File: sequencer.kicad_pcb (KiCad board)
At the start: 2 copper layers, 171.4 x 106.7 mm, 435 parts, among them J1 PJ301CM, J10 PJ301BM, J11 PJ301BM, J12 PJ301BM, J13 PJ301BM, J14 PJ301BM, J15 PJ301BM, J16 PJ301BM, J17 PJ301BM, J18 PJ301BM, J19 PJ301BM, J2 PJ301CM, J20 PJ301BM, J21 PJ301BM, J22 PJ301BM, J23 PJ301BM, J24 PJ301BM, J25 PJ301BM, J26 PJ301BM, J3 PJ301BM, J4 PJ301BM, J5 PJ301BM, J6 PJ301BM, J7 PJ301BM, J8 PJ301BM, J9 PJ301BM, Q1 MMBT3904, Q2 MMBT3904, Q3 MMBT3904, Q4 MMBT3904, Q5 MMBT3904, SW1 TL1105, SW10 TL1105, SW11 TL1105, SW12 TL1105, SW13 TL1105, SW14 TL1105, SW15 TL1105, SW16 TL1105, SW17 TL1105, SW18 TL1105, SW19 EVQQ2, SW2 TL1105, SW20 TL1105, SW21 TL1105, SW22 TL1105, SW23 TL1105, SW24 TL1105, SW25 TL1105, SW26 TL1105, SW27 TL1105, SW28 TL1105, SW29 TL1105, SW3 TL1105, SW30 TL1105, SW31 TL1105, SW32 TL1105, SW33 TL1105, SW34 TL1105, SW35 TL1105, SW36 TL1105, SW37 TL1105, SW38 TL1105, SW39 TL1105, SW4 TL1105, SW5 TL1105, SW6 TL1105, SW7 TL1105, SW8 EVQQ2, SW9 TL1105, U1 VO0600T, U10 LM1117-3.3, U11 74HC165, U12 74HC595, U13 74HC595, U14 74HC595, U15 OPA4172, U16 R-78E5.0-1.0, U2 74LV1T34, U3 STMPS2151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

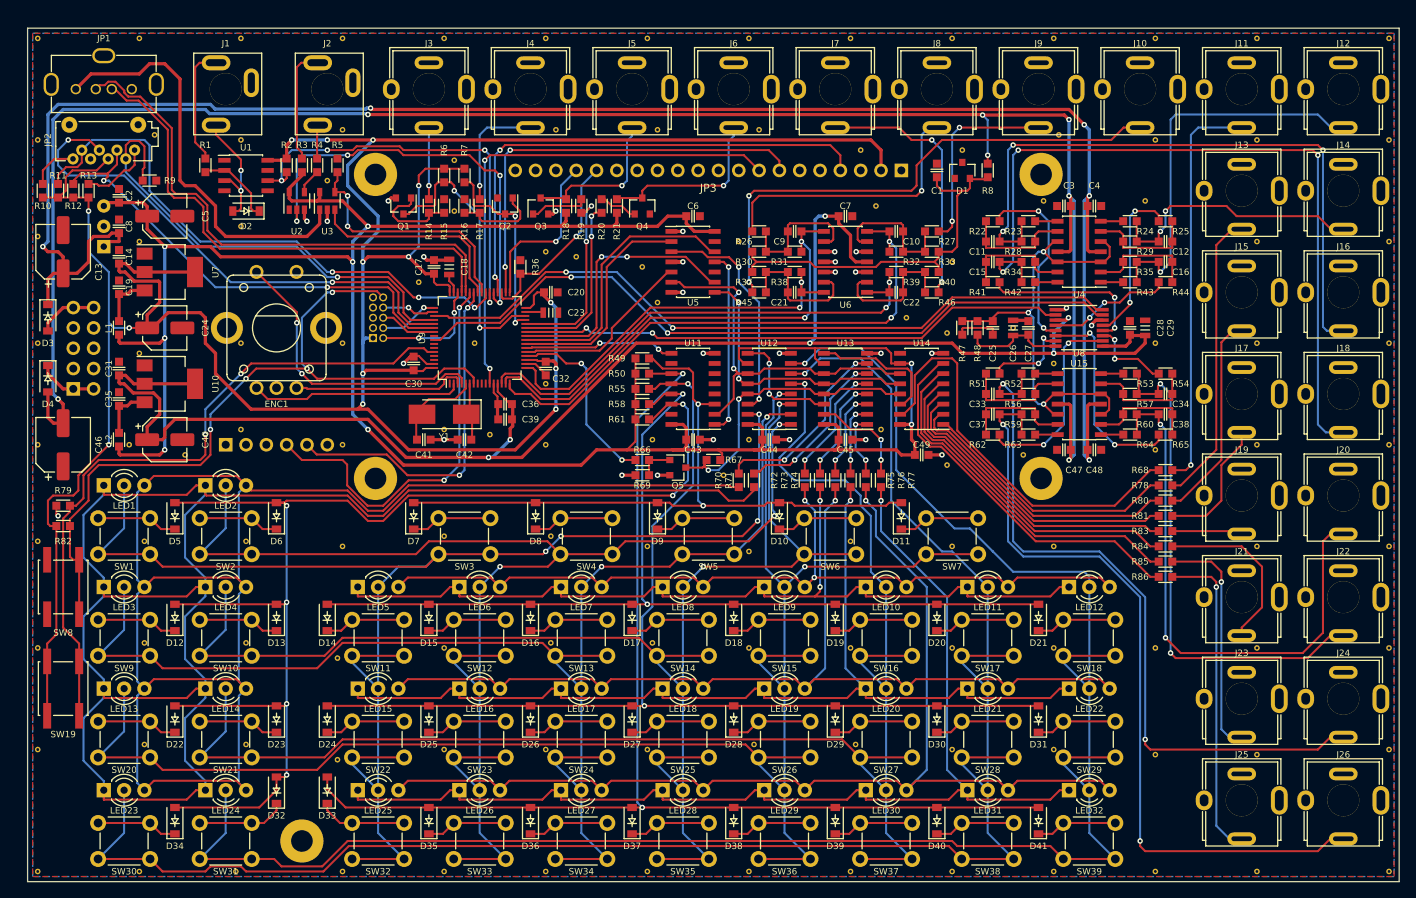
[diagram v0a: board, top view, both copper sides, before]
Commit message: Added solder jumpers for midi polarity and midi out/through.
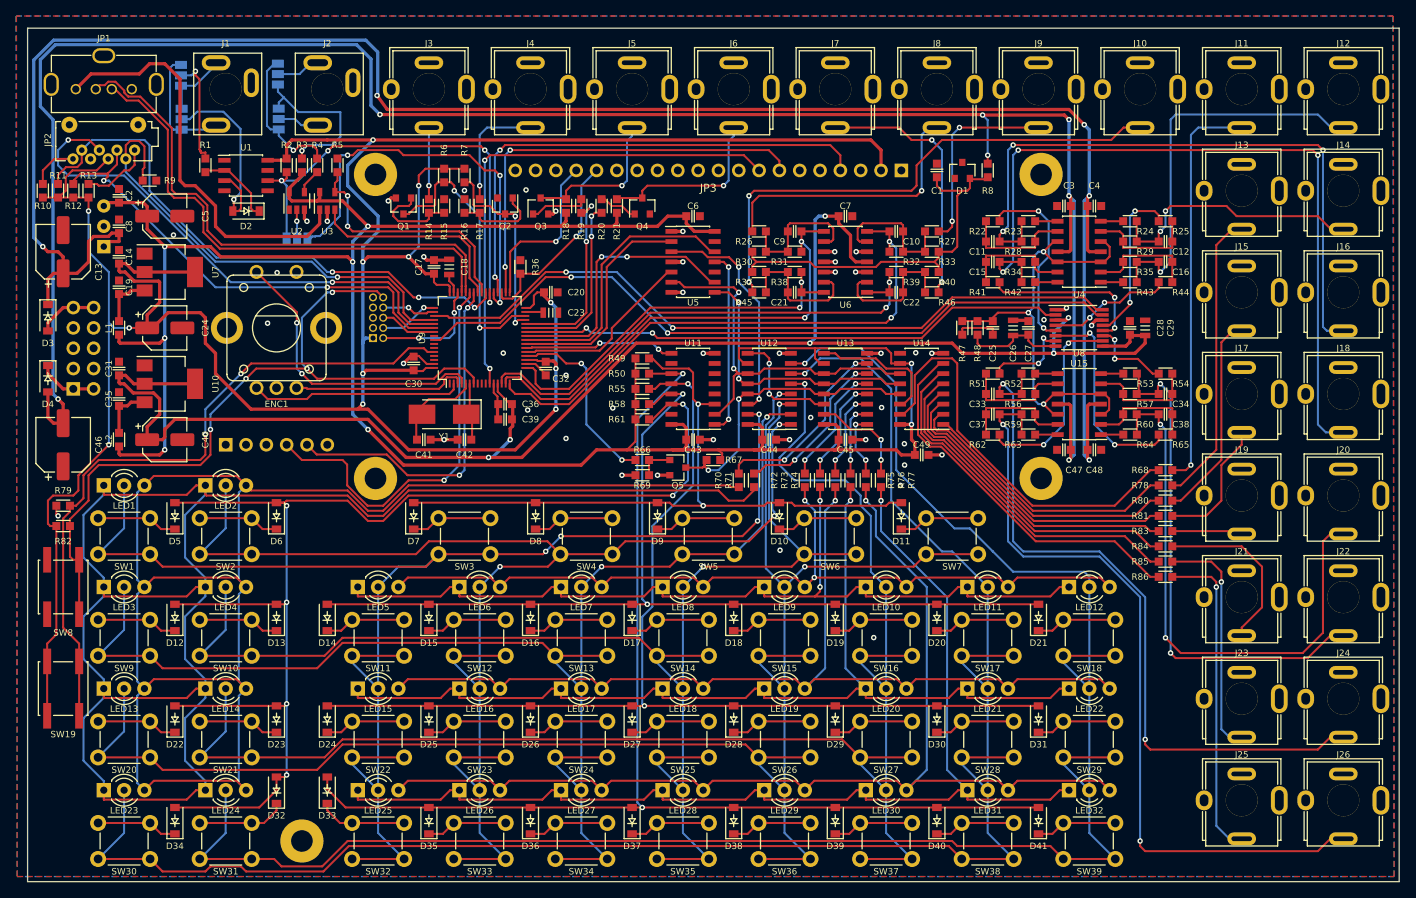
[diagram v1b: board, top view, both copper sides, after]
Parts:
- removed the REF** at (130.2, 61.0)
- removed the REF** at (205.1, 143.5)
- removed the REF** at (103.5, 62.9)
- removed the REF** at (90.8, 64.8)
- removed the REF** at (78.1, 64.1)
- removed the REF** at (247.0, 52.1)
- removed the REF** at (230.5, 52.1)
- removed the REF** at (217.8, 52.1)
- removed the REF** at (205.7, 51.4)
- removed the REF** at (193.7, 53.3)
- removed the REF** at (181.0, 53.3)
- removed the REF** at (168.3, 50.8)
- removed the REF** at (192.4, 143.5)
- removed the REF** at (155.6, 50.8)
- removed the REF** at (142.9, 50.8)
- removed the REF** at (130.2, 54.6)
- removed the REF** at (116.2, 50.8)
- removed the REF** at (103.5, 52.1)
- removed the REF** at (92.7, 51.4)
- removed the REF** at (78.1, 52.1)
- removed the REF** at (247.0, 39.4)
- removed the REF** at (230.5, 39.4)
- removed the REF** at (217.8, 39.4)
- removed the REF** at (179.7, 143.5)
- removed the REF** at (205.1, 39.4)
- removed the REF** at (192.4, 39.4)
- removed the REF** at (179.7, 39.4)
- removed the REF** at (167.0, 39.4)
- removed the REF** at (154.3, 39.4)
- removed the REF** at (141.6, 39.4)
- removed the REF** at (128.9, 39.4)
- removed the REF** at (116.2, 39.4)
- removed the REF** at (103.5, 39.4)
- removed the REF** at (90.8, 39.4)
- removed the REF** at (167.0, 143.5)
- removed the REF** at (78.1, 39.4)
- removed the REF** at (154.3, 143.5)
- removed the REF** at (141.6, 143.5)
- removed the REF** at (128.9, 143.5)
- removed the REF** at (116.2, 143.5)
- removed the REF** at (102.9, 143.5)
- removed the REF** at (90.8, 143.5)
- removed the REF** at (96.5, 91.4)
- removed the REF** at (78.1, 143.5)
- removed the REF** at (247.0, 128.3)
- removed the REF** at (230.5, 128.9)
- removed the REF** at (217.8, 128.9)
- removed the REF** at (205.1, 128.3)
- removed the REF** at (192.4, 128.3)
- removed the REF** at (180.3, 127.6)
- removed the REF** at (167.6, 127.6)
- removed the REF** at (154.3, 128.3)
- removed the REF** at (141.6, 128.3)
- removed the REF** at (134.6, 88.9)
- removed the REF** at (128.9, 128.3)
- removed the REF** at (115.6, 129.5)
- removed the REF** at (104.1, 127.6)
- removed the REF** at (91.4, 127.6)
- removed the REF** at (78.1, 128.3)
- removed the REF** at (247.0, 115.6)
- removed the REF** at (230.5, 115.6)
- removed the REF** at (217.8, 115.6)
- removed the REF** at (205.1, 115.6)
- removed the REF** at (192.4, 115.6)
- removed the REF** at (145.4, 66.7)
- removed the REF** at (179.7, 115.6)
- removed the REF** at (167.0, 115.6)
- removed the REF** at (154.9, 114.9)
- removed the REF** at (142.2, 114.9)
- removed the REF** at (128.9, 115.6)
- removed the REF** at (115.6, 116.8)
- removed the REF** at (104.1, 114.9)
- removed the REF** at (91.4, 114.9)
- removed the REF** at (78.1, 115.6)
- removed the REF** at (247.0, 102.9)
- removed the REF** at (200.0, 75.6)
- removed the REF** at (230.5, 102.9)
- removed the REF** at (205.1, 102.9)
- removed the REF** at (192.4, 102.9)
- removed the REF** at (179.7, 102.2)
- removed the REF** at (167.0, 103.5)
- removed the REF** at (154.3, 102.9)
- removed the REF** at (142.2, 101.6)
- removed the REF** at (128.9, 101.6)
- removed the REF** at (116.2, 102.9)
- removed the REF** at (104.1, 102.2)
- removed the REF** at (163.8, 94.0)
- removed the REF** at (91.4, 102.2)
- removed the REF** at (78.1, 102.2)
- removed the REF** at (247.0, 90.2)
- removed the REF** at (230.5, 90.2)
- removed the REF** at (217.8, 90.8)
- removed the REF** at (201.3, 91.4)
- removed the REF** at (191.8, 92.7)
- removed the REF** at (183.5, 88.3)
- removed the REF** at (167.0, 89.5)
- removed the REF** at (154.9, 89.5)
- removed the REF** at (247.0, 143.5)
- removed the REF** at (141.6, 90.2)
- removed the REF** at (128.9, 88.3)
- removed the REF** at (116.2, 90.2)
- removed the REF** at (103.5, 88.3)
- removed the REF** at (89.5, 90.2)
- removed the REF** at (78.1, 90.2)
- removed the REF** at (247.0, 77.5)
- removed the REF** at (230.5, 77.5)
- removed the REF** at (217.8, 77.5)
- removed the REF** at (205.1, 80.0)
- removed the REF** at (230.5, 143.5)
- removed the REF** at (191.8, 76.2)
- removed the REF** at (186.7, 74.3)
- removed the REF** at (155.6, 72.4)
- removed the REF** at (141.6, 82.5)
- removed the REF** at (132.7, 77.5)
- removed the REF** at (116.2, 77.5)
- removed the REF** at (103.5, 77.5)
- removed the REF** at (90.8, 78.7)
- removed the REF** at (78.1, 77.5)
- removed the REF** at (247.0, 64.8)
- removed the REF** at (217.8, 143.5)
- removed the REF** at (230.5, 64.8)
- removed the REF** at (216.5, 59.7)
- removed the REF** at (203.8, 59.7)
- removed the REF** at (192.4, 67.3)
- removed the REF** at (182.9, 60.3)
- removed the REF** at (165.7, 64.8)
- removed the REF** at (153.7, 67.9)
- removed the REF** at (141.6, 66.0)
- removed the REF** at (125.7, 69.8)
- removed the REF** at (114.3, 57.1)
- added JP10: korg/other, Jumper:SolderJumper-3_P1.3mm_Open_Pad1.0x1.5mm, B.Cu at (108.2, 49.5)
- added JP11: out/through, Jumper:SolderJumper-3_P1.3mm_Open_Pad1.0x1.5mm, B.Cu at (110.5, 64.4)
- added JP7: korg/other, Jumper:SolderJumper-3_P1.3mm_Open_Pad1.0x1.5mm, B.Cu at (96.0, 44.0)
- added JP8: korg/other, Jumper:SolderJumper-3_P1.3mm_Open_Pad1.0x1.5mm, B.Cu at (96.1, 49.5)
- added JP9: korg/other, Jumper:SolderJumper-3_P1.3mm_Open_Pad1.0x1.5mm, B.Cu at (108.1, 43.8)
- turned R4 to 270 degrees
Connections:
- J1 pad 1: Net-(J1-Pad1) -> (no net)
- J1 pad 3: Net-(D2-Pad2) -> Net-(J1-Pad3)
- J11 pad 2: Net-(J11-Pad2) -> (no net)
- J12 pad 2: Net-(J12-Pad2) -> (no net)
- J13 pad 2: Net-(J13-Pad2) -> (no net)
- J14 pad 2: Net-(J14-Pad2) -> (no net)
- J15 pad 2: Net-(J15-Pad2) -> (no net)
- J16 pad 2: Net-(J16-Pad2) -> (no net)
- J17 pad 2: Net-(J17-Pad2) -> (no net)
- J18 pad 2: Net-(J18-Pad2) -> (no net)
- J19 pad 2: Net-(J19-Pad2) -> (no net)
- J20 pad 2: Net-(J20-Pad2) -> (no net)
- J21 pad 2: Net-(J21-Pad2) -> (no net)
- J22 pad 2: Net-(J22-Pad2) -> (no net)
- J23 pad 2: Net-(J23-Pad2) -> (no net)
- J24 pad 2: Net-(J24-Pad2) -> (no net)
- J25 pad 2: Net-(J25-Pad2) -> (no net)
- J26 pad 2: Net-(J26-Pad2) -> (no net)
- J5 pad 2: Net-(J5-Pad2) -> (no net)
- J6 pad 2: Net-(J6-Pad2) -> (no net)
- JP3 pad 15: Net-(JP3-Pad15) -> (no net)
- JP3 pad 18: Net-(JP3-Pad18) -> (no net)
- JP3 pad 3: Net-(JP3-Pad3) -> (no net)
- JP3 pad 9: Net-(JP3-Pad9) -> (no net)
- JP4 pad 7: Net-(JP4-Pad7) -> (no net)
- JP6 pad 2: Net-(JP6-Pad2) -> (no net)
- JP6 pad 3: Net-(JP6-Pad3) -> (no net)
- JP6 pad 6: Net-(JP6-Pad6) -> (no net)
- R1 pad 2: Net-(J1-Pad2) -> Net-(JP7-Pad2)
- R3 pad 2: Net-(J2-Pad2) -> Net-(JP10-Pad1)
- R4 pad 1: Net-(R4-Pad1) -> Net-(JP10-Pad3)
- R4 pad 2: Net-(J2-Pad3) -> Net-(R4-Pad2)
- U1 pad 7: Net-(U1-Pad7) -> (no net)
- U11 pad 7: Net-(U11-Pad7) -> (no net)
- U14 pad 9: Net-(U14-Pad9) -> (no net)
- U2 pad 2: MIDI_TX -> Net-(JP11-Pad2)
- U2 pad 4: Net-(R4-Pad1) -> Net-(R4-Pad2)
- U9 pad 1: Net-(U9-Pad1) -> (no net)
- U9 pad 10: Net-(U9-Pad10) -> (no net)
- U9 pad 56: Net-(U9-Pad56) -> (no net)
- U9 pad 58: Net-(U9-Pad58) -> (no net)
- U9 pad 59: Net-(U9-Pad59) -> (no net)
- U9 pad 61: Net-(U9-Pad61) -> (no net)
- U9 pad 62: Net-(U9-Pad62) -> (no net)
- U9 pad 8: Net-(U9-Pad8) -> (no net)
- U9 pad 9: Net-(U9-Pad9) -> (no net)
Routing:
- net Net-(JP10-Pad1): track 0.00 -> 21.0 mm, vias 0 -> 1
- net Net-(JP10-Pad3): track 0.00 -> 18.1 mm, vias 0 -> 1
- net -12V: track 238.2 -> 255.0 mm
- net +12V: track 232.2 -> 248.2 mm
- net Net-(J1-Pad3): track 0.00 -> 15.8 mm
- net Net-(JP7-Pad2): track 0.00 -> 13.8 mm, vias 0 -> 1
- net Net-(D2-Pad2): track 15.9 -> 25.8 mm, vias 2 -> 1
- net Net-(J2-Pad2): track 14.5 -> 6.27 mm
- net Net-(J1-Pad2): track 14.8 -> 8.63 mm
- net MIDI_RX: track 52.7 -> 58.7 mm
- net Net-(JP11-Pad2): track 0.00 -> 3.61 mm, vias 0 -> 1
- net Net-(R4-Pad2): track 0.00 -> 3.15 mm
- net Net-(R4-Pad1): track 3.15 -> 0.00 mm
- net MIDI_TX: track 53.9 -> 52.0 mm, vias 4 -> 3
- net Net-(J2-Pad3): track 4.20 -> 5.29 mm
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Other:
- board text added: "MIDI <<<out through>>>"
- board text added: "korg >>>"

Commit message: Changed jack footprints to pj301cm.
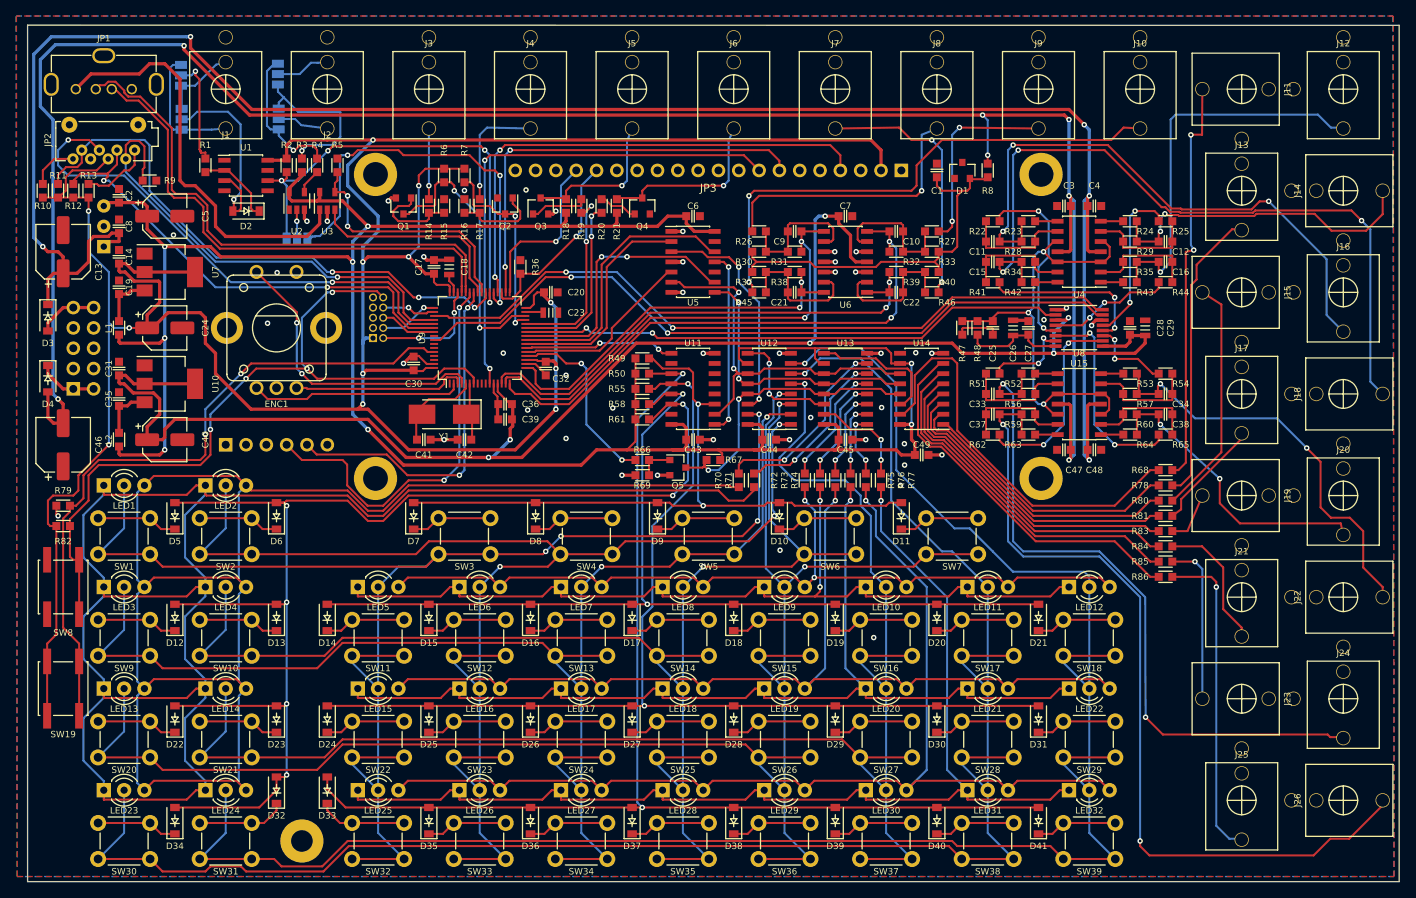
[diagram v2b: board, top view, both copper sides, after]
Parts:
- J1, J2: footprint w_connector:PJ301CM_OFFSET -> EuroCAD:PJ301M-12
- J10, J11, J12, J13, J14, J15, J16, J17, J18, J19, J20, J21, J22, J23, J24, J25, J26, J3, J4, J5, J6, J7, J8, J9: value PJ301BM -> PJ301M-12; footprint w_connector:PJ301BM -> EuroCAD:PJ301M-12
- turned J1 to 180 degrees
- turned J11 to 90 degrees
- turned J14 to 270 degrees
- turned J15 to 90 degrees
- turned J18 to 270 degrees
- turned J19 to 90 degrees
- turned J2 to 180 degrees
- turned J22 to 270 degrees
- turned J23 to 90 degrees
- turned J26 to 270 degrees
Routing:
- net CV5: track 70.5 -> 37.4 mm
- net CV6: track 63.5 -> 51.9 mm
- net CV3: track 83.9 -> 73.9 mm
- net Net-(J23-Pad3): track 29.3 -> 20.4 mm
- net CV2: track 33.1 -> 41.2 mm
- net CV8: track 98.4 -> 106.1 mm
- net CV4: track 99.7 -> 92.3 mm
- net Net-(J21-Pad3): track 21.9 -> 16.9 mm
- net Net-(J15-Pad3): track 26.3 -> 29.9 mm
- net CV7: track 90.5 -> 87.2 mm
- net -12V: track 255.0 -> 251.8 mm
- net Net-(J17-Pad3): track 16.5 -> 14.1 mm
- net Net-(J19-Pad3): track 9.06 -> 6.71 mm
- net +12V: track 248.2 -> 246.3 mm
- net Net-(J2-Pad3): track 5.29 -> 6.41 mm
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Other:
- board size 171.4 x 106.7 mm -> 171.4 x 107.1 mm
